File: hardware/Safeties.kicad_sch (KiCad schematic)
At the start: 20 parts, among them K2 6-1419128-4, Q2 2N7002, Q4 2N7002, Q8 AO3400A, U14 74AUP1G32, U8 74LVC1G86

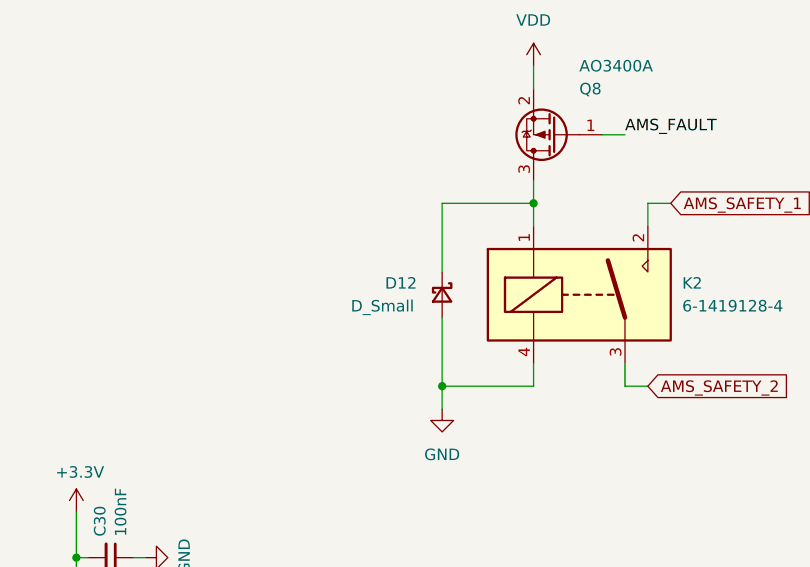
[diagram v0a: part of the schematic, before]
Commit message: symbol update
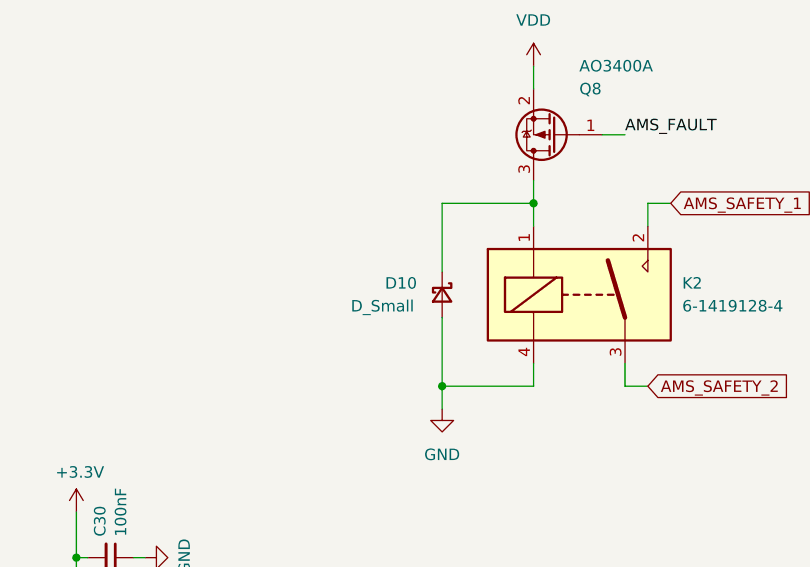
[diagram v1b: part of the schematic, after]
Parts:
- renumbered D12 to D10
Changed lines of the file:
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@@
   (symbol (lib_id "Device:D_Schottky_Small") (at 212.09 81.28 270) (unit 1)
     (in_bom yes) (on_board yes) (dnp no)
-    (property "Reference" "D12" (at 205.74 80.01 90)
+    (property "Reference" "D10" (at 205.74 80.01 90)
       (effects (font (size 1.27 1.27)) (justify left))
     )
@@
     (instances
       (project "PUTM_EV_BMS_HV_Master_2021"
-        (path "/b456cffc-d9d7-4c91-91f2-36ec9a65dd1b/6eb4a2b1-8e5b-451b-b593-8aaaa3a4213e/649ea10f-ddf7-49be-afe9-7c2c999df872"
-          (reference "D12") (unit 1)
-        )
-        (path "/b456cffc-d9d7-4c91-91f2-36ec9a65dd1b/6eb4a2b1-8e5b-451b-b593-8aaaa3a4213e/67d08ddd-b8e9-4f40-a055-93108463bf84"
-          (reference "D4") (unit 1)
-        )
-        (path "/b456cffc-d9d7-4c91-91f2-36ec9a65dd1b/6eb4a2b1-8e5b-451b-b593-8aaaa3a4213e/fd8c1b79-afed-4653-bb63-44888bf7ecb3"
-          (reference "D13") (unit 1)
-        )
         (path "/b456cffc-d9d7-4c91-91f2-36ec9a65dd1b/6eb4a2b1-8e5b-451b-b593-8aaaa3a4213e"
           (reference "D10") (unit 1)

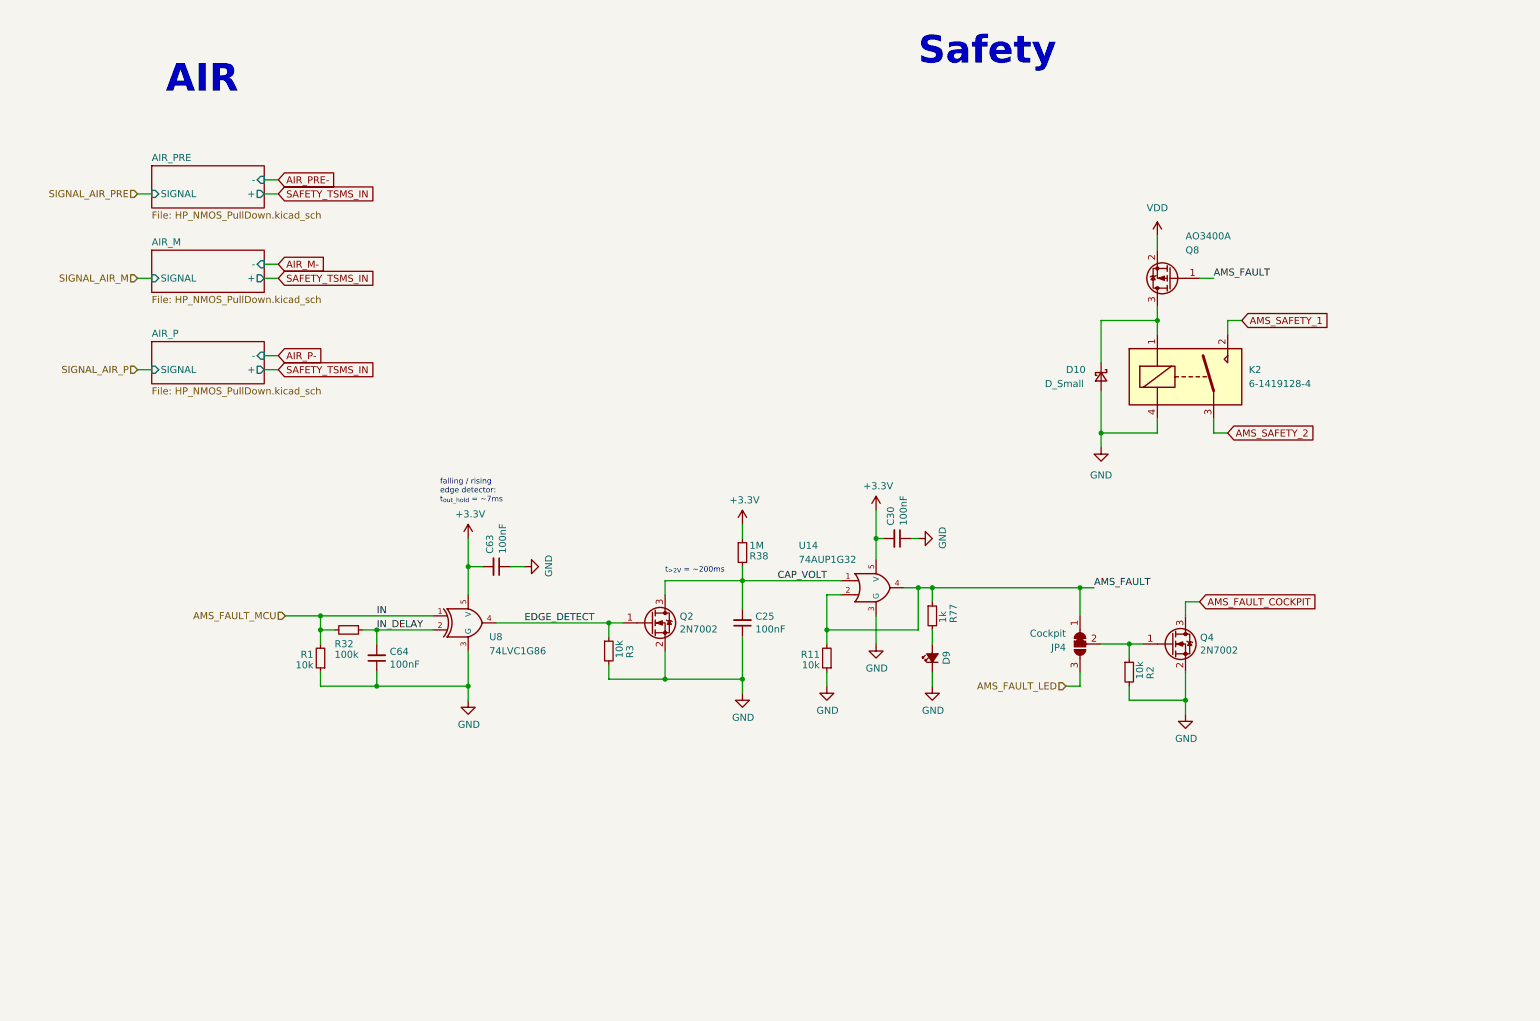
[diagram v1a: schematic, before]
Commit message: schematic clean up
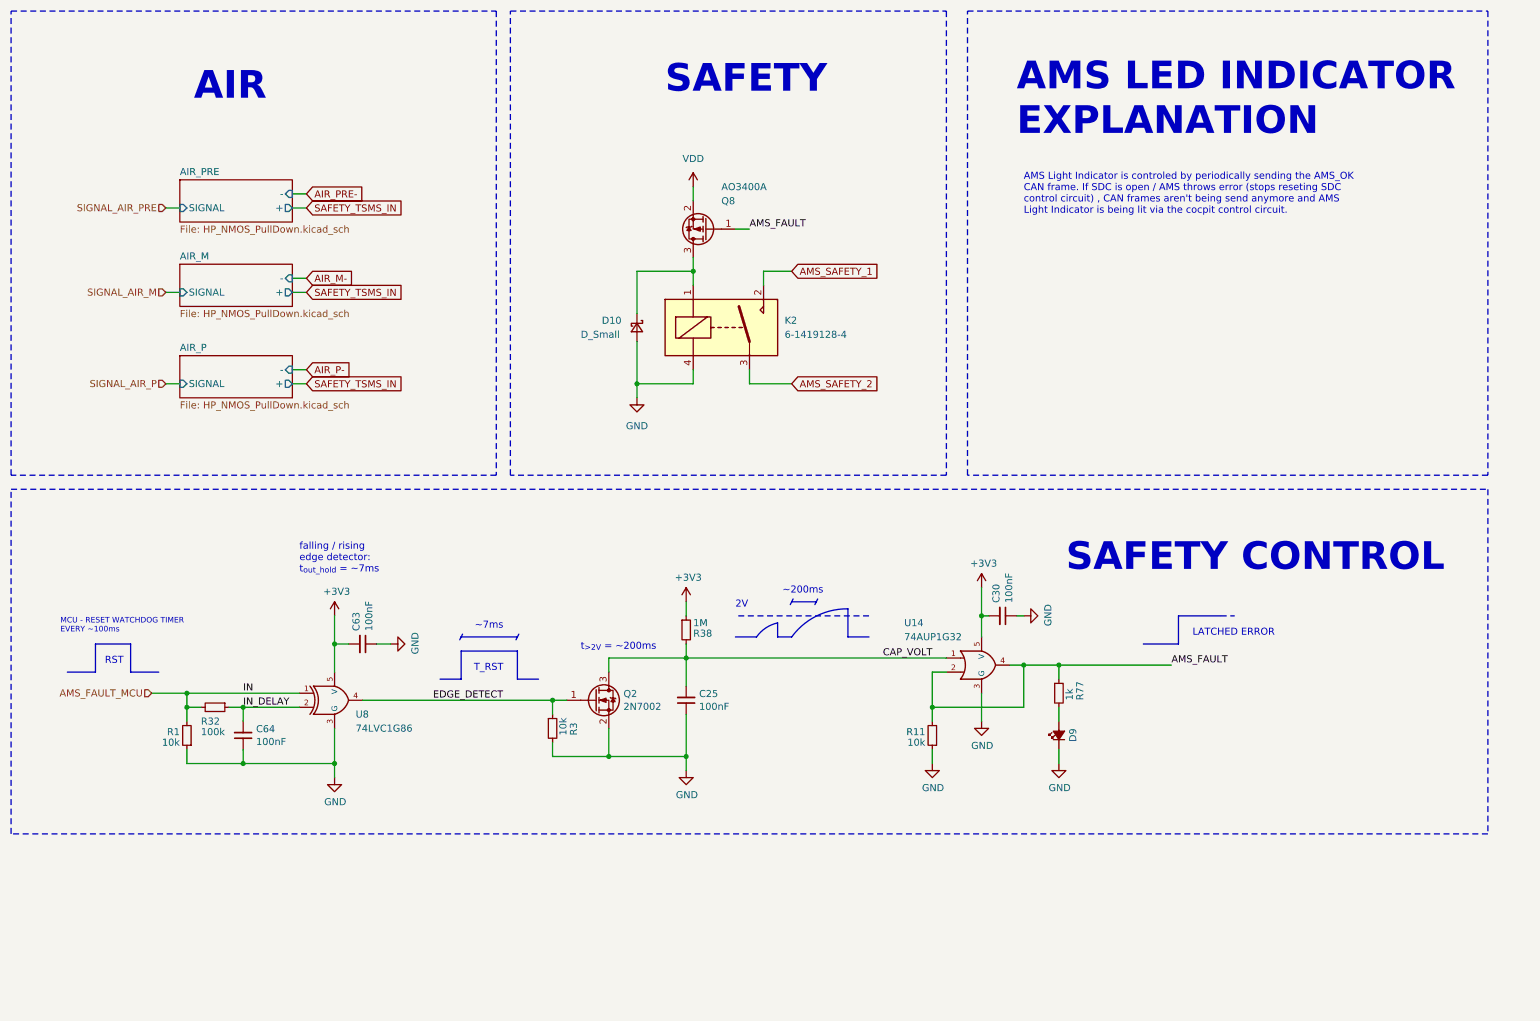
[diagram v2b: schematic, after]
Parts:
- removed JP4: Cockpit, Jumper:SolderJumper-3_P1.3mm_Bridged12_RoundedPad1.0x1.5mm, symbol Jumper:SolderJumper_3_Bridged12
- removed Q4: 2N7002, Package_TO_SOT_SMD:SOT-23, symbol Transistor_FET:2N7002
- removed R2: 10k, Resistor_SMD:R_0603_1608Metric, symbol Device:R_Small
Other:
- note added: "2V"
- note added: "AMS LED INDICATOR EXPLANATION"
- note added: "AMS Light Indicator is controled by periodically sending the AMS_OK CAN frame. If SDC is open / AMS throws error (stops reseting SDC control circuit) , CAN frames aren't being send anymore and AMS Light Indicator is being lit via the cocpit control circuit."
- note added: "LATCHED ERROR"
- note added: "MCU - RESET WATCHDOG TIMER EVERY ~100ms"
- note added: "RST"
- note added: "SAFETY"
- note added: "SAFETY CONTROL"
- note added: "T_RST"
- note added: "~200ms"
- note added: "~7ms"
- note removed: "Safety"
- title: (none) -> AMS
- moved on the sheet: C25, C30, C63, C64, D10, D9, K2, Q2, Q8, R1, R11, R3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

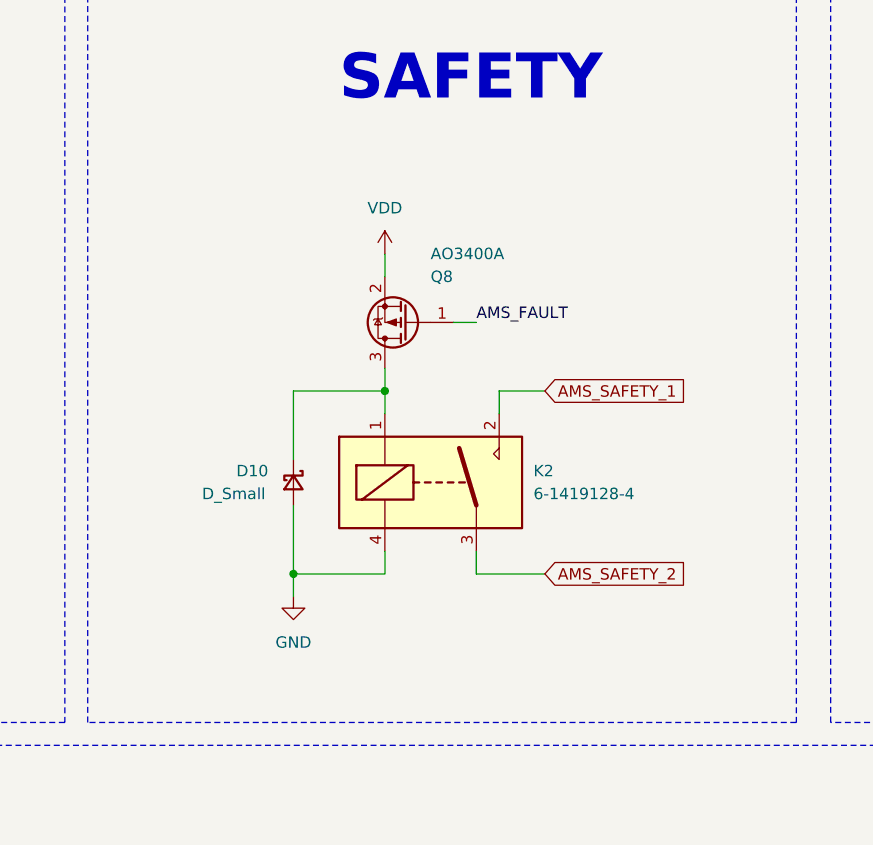
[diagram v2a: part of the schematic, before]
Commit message: relay new driving logic, some ltc communication changes
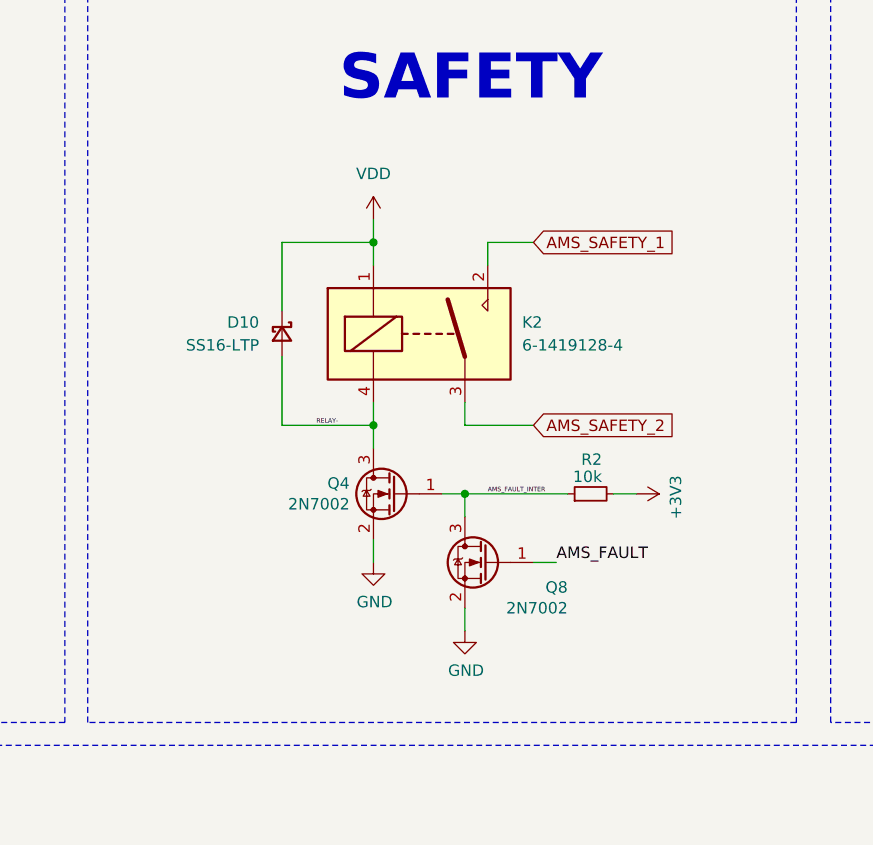
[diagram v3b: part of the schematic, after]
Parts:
- removed Q8: AO3400A, Package_TO_SOT_SMD:SOT-23, symbol Device:Q_PMOS_GSD
- added Q4, Q8: 2N7002, Package_TO_SOT_SMD:SOT-23, symbol Transistor_FET:2N7002
- added R2: 10k, Resistor_SMD:R_0603_1608Metric, symbol Device:R_Small
- D10: value D_Small -> SS16-LTP
- D9: value LED_Small_ALT -> SML-D12U1WT86
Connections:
- net +3V3: now also R2.2
- net AMS_FAULT: now also Q8.1 (G)
- net GND: now also Q4.2 (S), Q8.2 (S); no longer D10.2 (A), K2.4
- net VDD: now also D10.1 (K), K2.1
- new net AMS_FAULT_INTER: Q4.1 (G), Q8.3 (D), R2.1
- new net RELAY-: D10.2 (A), K2.4, Q4.3 (D)
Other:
- moved on the sheet: D10, K2

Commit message: relay new driving logic, some ltc communication changes
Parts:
- renumbered C64 to C5, C63 to C6, C25 to C7, C30 to C8, D10 to D7, D9 to D8, K2 to K1, Q2 to Q1, Q4 to Q2, Q8 to Q3, R32 to R10, R3 to R11, R38 to R12, R2 to R13, R11 to R14, R77 to R15, R1 to R9, U8 to U2, U14 to U3

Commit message: major schematic changes
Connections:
- net AMS_FAULT_INTER renamed AMS_OK
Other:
- removed sheet AIR_M
- removed sheet AIR_P
- removed sheet AIR_PRE
- note removed: "AIR"
- moved on the sheet: D7, K1, Q2, Q3, R13

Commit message: fixed some footprints; shorted pcb board to 60x100; re-designed the HV & current measuring as well as LTC communication, all are in one TS section;
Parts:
- D7: footprint Diode_SMD:D_SMA -> Diode_SMD:D_SOD-123
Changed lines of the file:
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@@
 			)
 		)
-		(property "Footprint" "Diode_SMD:D_SMA"
+		(property "Footprint" "Diode_SMD:D_SOD-123"
 			(at 46.99 54.61 90)
 			(effects

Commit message: changes tbc
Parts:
- removed K1: 6-1419128-4, 614191284, symbol 6-1419128-4:6-1419128-4
- added K2: PB134024, Samacsys:PB134024, symbol Samacsys_kicad_sym:PB134024
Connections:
- net AMS_SAFETY_1: now also K2.14 (NO)
- net AMS_SAFETY_2: now also K2.11 (COM)
- net RELAY-: now also K2.A1 (COIL_1)
- net VDD: now also K2.A2 (COIL_2)
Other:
- moved on the sheet: D7, Q2, Q3, R13
